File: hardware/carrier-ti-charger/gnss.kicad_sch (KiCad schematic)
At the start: 28 parts, among them J13 GNSS_ANT, Q14 AO3401A, Q15 2N7002, Q16 2N7002, SW5 ACTIVE_ANT, U16 MAX-M10S-00B, U17 TLV9001IDBVR, U18 TPS7A0233PDBVR

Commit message: Fix missing parts.
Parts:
- D11: footprint Diode_SMD:D_0402_1005Metric -> carrier:D_0402_1005Metric
- D12: value BAT54WS -> 1N4148WS; LCSC C22629 -> C2128; MPN BAT54WS -> 1N4148WS
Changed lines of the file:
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@@
 			)
 		)
-		(property "Value" "BAT54WS"
+		(property "Value" "1N4148WS"
 			(at 116.84 41.91 0)
 			(show_name no)
@@
 			)
 		)
-		(property "LCSC" "C22629"
+		(property "LCSC" "C2128"
 			(at 119.38 48.26 0)
 			(hide yes)
@@
 			)
 		)
-		(property "MPN" "BAT54WS"
+		(property "MPN" "1N4148WS"
 			(at 119.38 48.26 0)
 			(hide yes)
@@
 			)
 		)
-		(property "Footprint" "Diode_SMD:D_0402_1005Metric"
+		(property "Footprint" "carrier:D_0402_1005Metric"
 			(at 195.58 107.95 0)
 			(hide yes)

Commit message: Consolidate bom.
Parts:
- C60, C61: value 100n 50V -> 100n 16V; footprint Capacitor_SMD:C_0603_1608Metric -> carrier:C_0402_1005Metric_NoSilk; LCSC C14663 -> C1525; MPN CC0603KRX7R9BB104 -> CL05B104KO5NNNC
- D14: value CT-1608DUPC-P6 -> KT-0603W white; LCSC C52676000 -> C2290; MPN CT-1608DUPC-P6 -> KT-0603W
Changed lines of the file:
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@@
 			)
 		)
-		(property "Value" "100n 50V"
+		(property "Value" "100n 16V"
 			(at 104.14 81.28 0)
 			(show_name no)
@@
 			)
 		)
-		(property "Footprint" "Capacitor_SMD:C_0603_1608Metric"
+		(property "Footprint" "carrier:C_0402_1005Metric_NoSilk"
 			(at 101.6 80.01 0)
 			(hide yes)
@@
 			)
 		)
-		(property "LCSC" "C14663"
+		(property "LCSC" "C1525"
 			(at 101.6 80.01 0)
 			(hide yes)
@@
 			)
 		)
-		(property "MPN" "CC0603KRX7R9BB104"
+		(property "MPN" "CL05B104KO5NNNC"
 			(at 101.6 80.01 0)
 			(hide yes)
@@
 			)
 		)
-		(property "Value" "100n 50V"
+		(property "Value" "100n 16V"
 			(at 231.14 157.48 0)
 			(show_name no)
@@
 			)
 		)
-		(property "Footprint" "Capacitor_SMD:C_0603_1608Metric"
+		(property "Footprint" "carrier:C_0402_1005Metric_NoSilk"
 			(at 228.6 156.21 0)
 			(hide yes)
@@
 			)
 		)
-		(property "LCSC" "C14663"
+		(property "LCSC" "C1525"
 			(at 228.6 156.21 0)
 			(hide yes)
@@
 			)
 		)
-		(property "MPN" "CC0603KRX7R9BB104"
+		(property "MPN" "CL05B104KO5NNNC"
 			(at 228.6 156.21 0)
 			(hide yes)
@@
 			)
 		)
-		(property "Value" "CT-1608DUPC-P6"
+		(property "Value" "KT-0603W white"
 			(at 86.36 152.4 90)
 			(show_name no)
@@
 			)
 		)
-		(property "Description" "Fix LED, purple, blinks with PPS"
+		(property "Description" "Fix LED, white, blinks with PPS"
 			(at 83.82 151.13 0)
 			(hide yes)
@@
 			)
 		)
-		(property "LCSC" "C52676000"
+		(property "LCSC" "C2290"
 			(at 83.82 151.13 0)
 			(hide yes)
@@
 			)
 		)
-		(property "MPN" "CT-1608DUPC-P6"
+		(property "MPN" "KT-0603W"
 			(at 83.82 151.13 0)
 			(hide yes)

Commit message: Address review findings.
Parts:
- R82: LCSC C17415 -> C727983; MPN 0805W8F100JT5E -> AC0805FR-7W10RL
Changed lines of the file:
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@@
 			)
 		)
-		(property "Description" "Antenna current sense and short limit (UBX-20053088 R8)"
+		(property "Description" "Antenna current sense and short limit, 0.25 W (UBX-20053088 R8)"
 			(at 185.42 132.08 0)
 			(hide yes)
@@
 			)
 		)
-		(property "LCSC" "C17415"
+		(property "LCSC" "C727983"
 			(at 185.42 132.08 0)
 			(hide yes)
@@
 			)
 		)
-		(property "MPN" "0805W8F100JT5E"
+		(property "MPN" "AC0805FR-7W10RL"
 			(at 185.42 132.08 0)
 			(hide yes)

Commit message: Polishing.
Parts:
- renumbered J13 to J7, JP4 to JP2

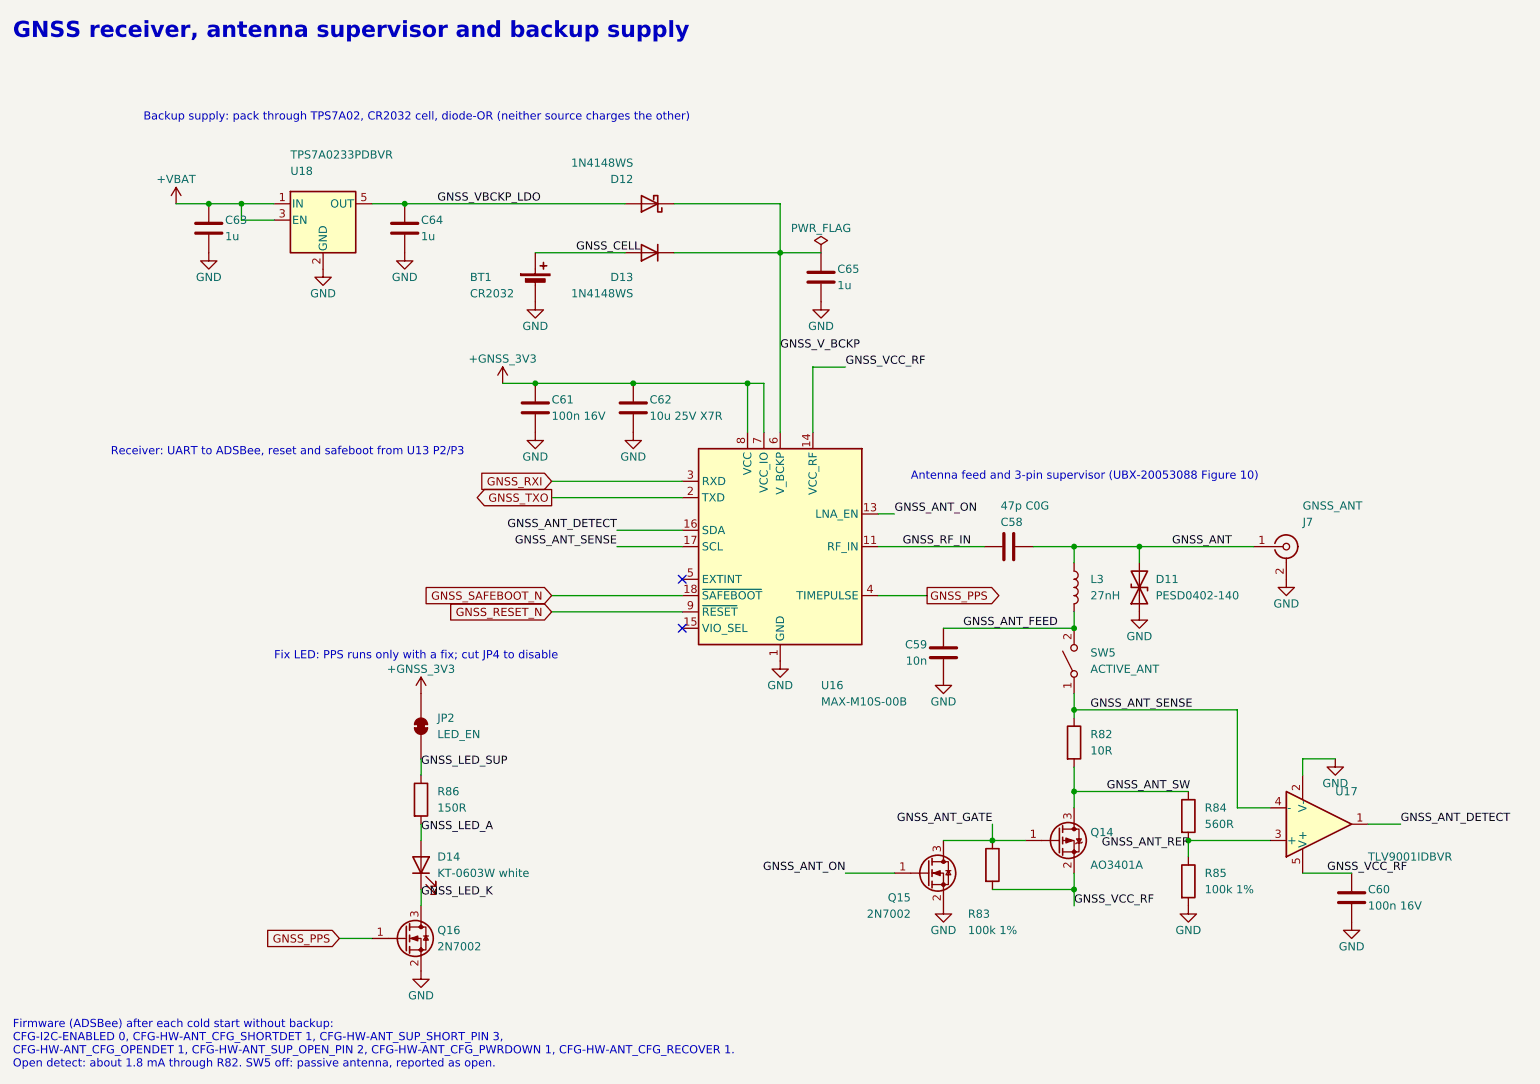
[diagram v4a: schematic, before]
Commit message: Consolidate BOM, add GNSS listen to ESP.
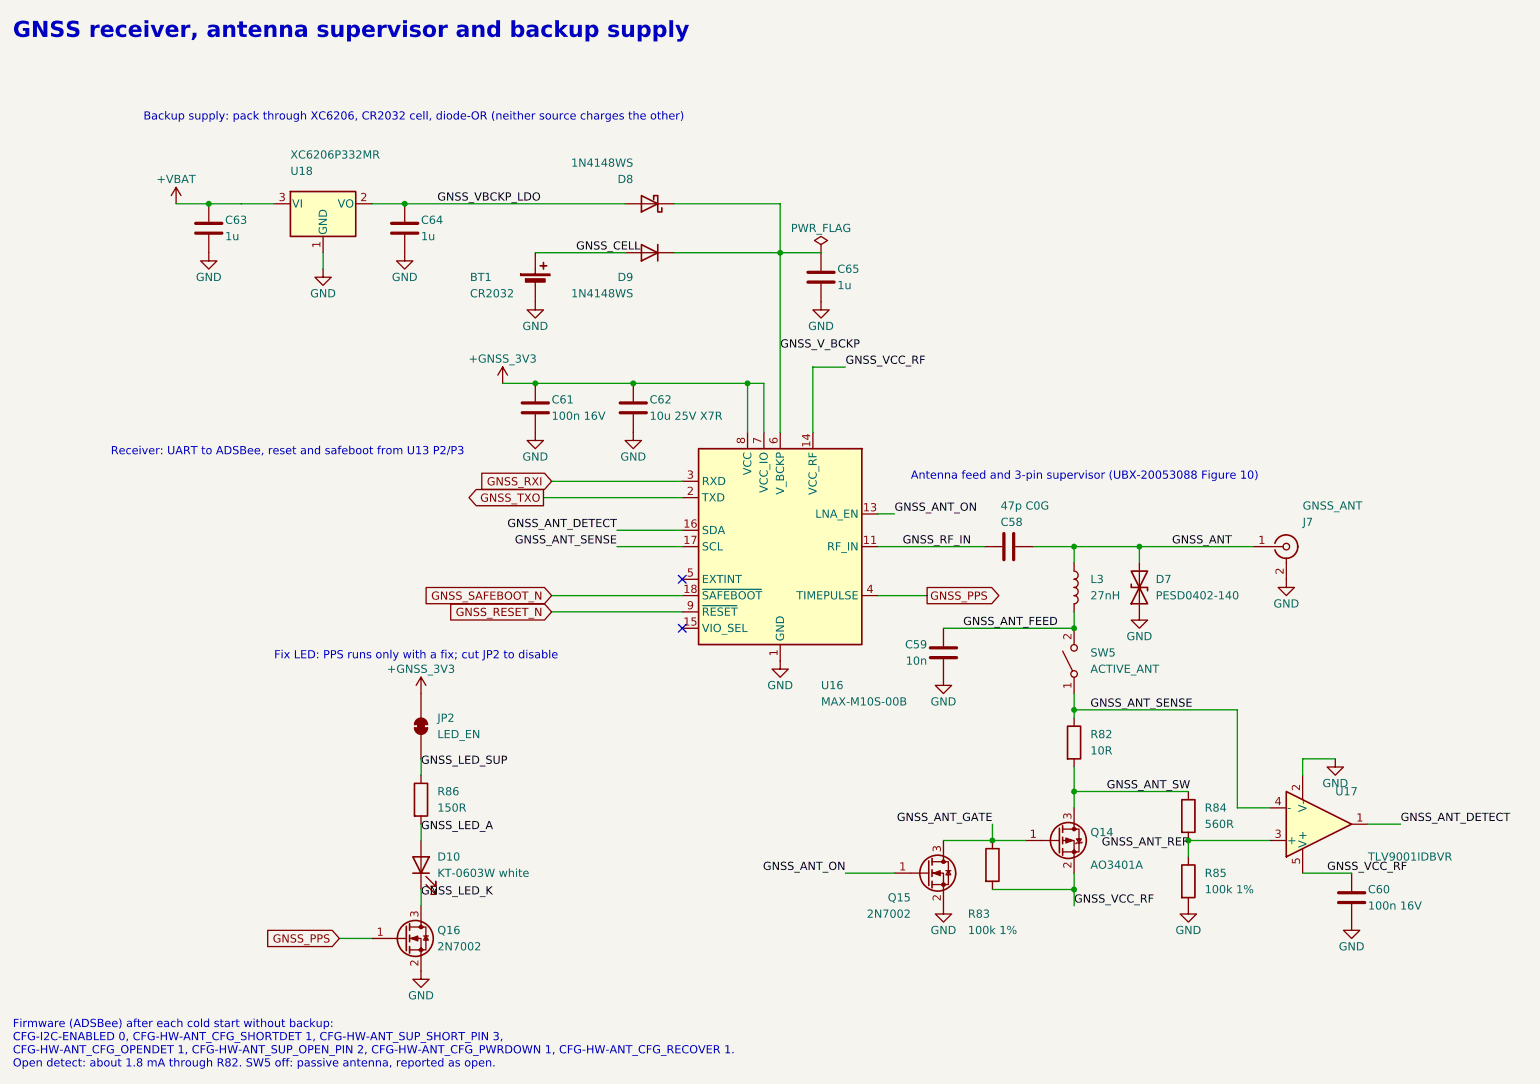
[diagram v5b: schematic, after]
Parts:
- removed U18: TPS7A0233PDBVR, Package_TO_SOT_SMD:SOT-23-5, symbol carrier:TPS7A0233PDBV
- added U18: XC6206P332MR, Package_TO_SOT_SMD:SOT-23, symbol Mark:XC6206P332MR
- BT1: footprint carrier:BAT-SMD_BS-CR2032-8 -> Mark:BAT-SMD_BS-CR2032-8
- C58, C60, C61: footprint carrier:C_0402_1005Metric_NoSilk -> Mark:C_0402_1005Metric_NoSilk
- D7: renamed from D11; footprint carrier:D_0402_1005Metric -> Mark:D_0402_1005Metric
- J7: footprint carrier:U.FL_Hirose_U.FL-R-SMT-1_Vertical -> Mark:U.FL_Hirose_U.FL-R-SMT-1_Vertical
- R82: footprint carrier:R_0805_2012Metric_NoSilk -> Mark:R_0805_2012Metric_NoSilk
- SW5: footprint carrier:SW-SMD_SHOUHAN_2.54-1P_TPGT -> Mark:SW-SMD_SHOUHAN_2.54-1P_TPGT
- U16: footprint carrier:ublox_MAX-M10S -> Mark:ublox_MAX-M10S
- U17: symbol carrier:TLV9001IDBV -> Mark:TLV9001IDBV
- renumbered D14 to D10, D12 to D8, D13 to D9
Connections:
- net +VBAT: now also U18.3 (VI)
- net GND: now also U18.1 (GND)
- net GNSS_VBCKP_LDO: now also U18.2 (VO)
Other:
- note added: "Backup supply: pack through XC6206, CR2032 cell, diode-OR (neither source charges the other)"
- note added: "Fix LED: PPS runs only with a fix; cut JP2 to disable"
- note removed: "Backup supply: pack through TPS7A02, CR2032 cell, diode-OR (neither source charges the other)"
- note removed: "Fix LED: PPS runs only with a fix; cut JP4 to disable"
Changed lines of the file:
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@@
 		)
 	)
-	(text "Backup supply: pack through TPS7A02, CR2032 cell, diode-OR (neither source charges the other)"
+	(text "Backup supply: pack through XC6206, CR2032 cell, diode-OR (neither source charges the other)"
 		(exclude_from_sim no)
 		(at 40.64 35.56 0)
@@
 		)
 	)
-	(text "Fix LED: PPS runs only with a fix; cut JP4 to disable"
+	(text "Fix LED: PPS runs only with a fix; cut JP2 to disable"
 		(exclude_from_sim no)
 		(at 60.96 119.38 0)
@@
 	)
 	(junction
-		(at 55.88 48.26)
-		(diameter 0)
-		(color 0 0 0 0)
-	)
-	(junction
 		(at 50.8 48.26)
 		(diameter 0)
@@
 	(wire
 		(pts
-			(xy 104.14 93.98) (xy 124.46 93.98)
+			(xy 102.87 93.98) (xy 124.46 93.98)
 		)
 		(stroke
@@
 	(wire
 		(pts
-			(xy 55.88 50.8) (xy 60.96 50.8)
-		)
-		(stroke
-			(width 0)
-			(type default)
-		)
-	)
-	(wire
-		(pts
 			(xy 179.07 101.6) (xy 185.42 101.6)
 		)
@@
 	(wire
 		(pts
-			(xy 55.88 48.26) (xy 55.88 50.8)
-		)
-		(stroke
-			(width 0)
-			(type default)
-		)
-	)
-	(wire
-		(pts
 			(xy 124.46 101.6) (xy 114.3 101.6)
 		)
@@
 	(global_label "GNSS_TXO"
 		(shape output)
-		(at 104.14 93.98 180)
+		(at 102.87 93.98 180)
 		(fields_autoplaced yes)
 		(effects
@@
 		)
 		(property "Intersheetrefs" "${INTERSHEET_REFS}"
-			(at 104.14 93.98 0)
+			(at 102.87 93.98 0)
 			(hide yes)
 			(show_name no)
@@
 	)
 	(symbol
-		(lib_id "carrier:+GNSS_3V3")
+		(lib_id "Mark:+GNSS_3V3")
 		(at 83.82 124.46 0)
 		(unit 1)
@@
 			)
 		)
-		(property "Footprint" "carrier:ublox_MAX-M10S"
+		(property "Footprint" "Mark:ublox_MAX-M10S"
 			(at 139.7 101.6 0)
 			(hide yes)
@@
 		(in_pos_files yes)
 		(dnp no)
-		(property "Reference" "D12"
+		(property "Reference" "D8"
 			(at 116.84 44.45 0)
 			(show_name no)
@@
 			(project "carrier"
 				(path "/1d76d2ec-7795-4c71-8167-b1182c3ebc1d/a06322b6-1276-4059-95cd-666fc3516e91"
-					(reference "D12")
+					(reference "D8")
 					(unit 1)
 				)
@@
 	)
 	(symbol
-		(lib_id "carrier:+GNSS_3V3")
+		(lib_id "Mark:+GNSS_3V3")
 		(at 96.52 76.2 0)
 		(unit 1)
@@
 	)
 	(symbol
-		(lib_id "carrier:TLV9001IDBV")
+		(lib_id "Mark:TLV9001IDBV")
 		(at 223.52 144.78 0)
 		(mirror x)
@@
 		(in_pos_files yes)
 		(dnp no)
-		(property "Reference" "D11"
+		(property "Reference" "D7"
 			(at 198.12 106.68 90)
 			(show_name no)
@@
 			)
 		)
-		(property "Footprint" "carrier:D_0402_1005Metric"
+		(property "Footprint" "Mark:D_0402_1005Metric"
 			(at 195.58 107.95 0)
 			(hide yes)
@@
 			(project "carrier"
 				(path "/1d76d2ec-7795-4c71-8167-b1182c3ebc1d/a06322b6-1276-4059-95cd-666fc3516e91"
-					(reference "D11")
+					(reference "D7")
 					(unit 1)
 				)
@@
 	)
 	(symbol
-		(lib_id "carrier:TPS7A0233PDBV")
-		(at 68.58 50.8 0)
-		(unit 1)
-		(body_style 1)
-		(exclude_from_sim no)
-		(in_bom yes)
-		(on_board yes)
-		(in_pos_files yes)
-		(dnp no)
-		(property "Reference" "U18"
-			(at 63.5 43.18 0)
-			(show_name no)
-			(do_not_autoplace no)
-			(effects
-				(font
-					(size 1.27 1.27)
-				)
-				(justify left)
-			)
-		)
-		(property "Value" "TPS7A0233PDBVR"
-			(at 63.5 40.64 0)
-			(show_name no)
-			(do_not_autoplace no)
-			(effects
-				(font
-					(size 1.27 1.27)
-				)
-				(justify left)
-			)
-		)
-		(property "Footprint" "Package_TO_SOT_SMD:SOT-23-5"
-			(at 68.58 50.8 0)
-			(hide yes)
-			(show_name no)
-			(do_not_autoplace no)
-			(effects
-				(font
-					(size 1.27 1.27)
-				)
-			)
-		)
-		(property "Datasheet" "https://www.ti.com/lit/ds/symlink/tps7a02.pdf"
-			(at 68.58 50.8 0)
-			(hide yes)
-			(show_name no)
-			(do_not_autoplace no)
-			(effects
-				(font
-					(size 1.27 1.27)
-				)
-			)
-		)
-		(property "Description" "Always-on 3.3 V backup supply from the pack, 25 nA quiescent"
-			(at 68.58 50.8 0)
-			(hide yes)
-			(show_name no)
-			(do_not_autoplace no)
-			(effects
-				(font
-					(size 1.27 1.27)
-				)
-			)
-		)
-		(property "LCSC" "C2887324"
-			(at 68.58 50.8 0)
-			(hide yes)
-			(show_name no)
-			(do_not_autoplace no)
-			(effects
-				(font
-					(size 1.27 1.27)
-				)
-			)
-		)
-		(property "MPN" "TPS7A0233PDBVR"
-			(at 68.58 50.8 0)
-			(hide yes)
-			(show_name no)
-			(do_not_autoplace no)
-			(effects
-				(font
-					(size 1.27 1.27)
-				)
-			)
-		)
-		(property "Manufacturer" "Texas Instruments"
-			(at 68.58 50.8 0)
-			(hide yes)
-			(show_name no)
-			(do_not_autoplace no)
-			(effects
-				(font
-					(size 1.27 1.27)
-				)
-			)
-		)
-		(pin "1"
-		)
-		(pin "2"
-		)
-		(pin "3"
-		)
-		(pin "4"
-		)
-		(pin "5"
-		)
-		(instances
-			(project "carrier"
-				(path "/1d76d2ec-7795-4c71-8167-b1182c3ebc1d/a06322b6-1276-4059-95cd-666fc3516e91"
-					(reference "U18")
-					(unit 1)
-				)
-			)
-		)
-	)
-	(symbol
 		(lib_id "Device:R")
 		(at 185.42 132.08 0)
@@
 			)
 		)
-		(property "Footprint" "carrier:R_0805_2012Metric_NoSilk"
+		(property "Footprint" "Mark:R_0805_2012Metric_NoSilk"
 			(at 185.42 132.08 0)
 			(hide yes)
@@
 	)
 	(symbol
-		(lib_id "carrier:+VBAT")
+		(lib_id "Mark:+VBAT")
 		(at 45.72 48.26 0)
 		(unit 1)
@@
 			)
 		)
-		(property "Footprint" "carrier:C_0402_1005Metric_NoSilk"
+		(property "Footprint" "Mark:C_0402_1005Metric_NoSilk"
 			(at 101.6 80.01 0)
 			(hide yes)
@@
 			)
 		)
-		(property "Footprint" "carrier:U.FL_Hirose_U.FL-R-SMT-1_Vertical"
+		(property "Footprint" "Mark:U.FL_Hirose_U.FL-R-SMT-1_Vertical"
 			(at 218.44 101.6 0)
 			(hide yes)
@@
 			)
 		)
-		(property "Footprint" "carrier:C_0402_1005Metric_NoSilk"
+		(property "Footprint" "Mark:C_0402_1005Metric_NoSilk"
 			(at 228.6 156.21 0)
 			(hide yes)
@@
 		(in_pos_files yes)
 		(dnp no)
-		(property "Reference" "D14"
+		(property "Reference" "D10"
 			(at 86.36 149.86 90)
 			(show_name no)
@@
 			(project "carrier"
 				(path "/1d76d2ec-7795-4c71-8167-b1182c3ebc1d/a06322b6-1276-4059-95cd-666fc3516e91"
-					(reference "D14")
+					(reference "D10")
 					(unit 1)
 				)
@@
 			)
 		)
-		(property "Footprint" "carrier:BAT-SMD_BS-CR2032-8"
+		(property "Footprint" "Mark:BAT-SMD_BS-CR2032-8"
 			(at 101.6 60.96 0)
 			(hide yes)
@@
 			)
 		)
-		(property "Footprint" "carrier:C_0402_1005Metric_NoSilk"
+		(property "Footprint" "Mark:C_0402_1005Metric_NoSilk"
 			(at 175.26 101.6 0)
 			(hide yes)
@@
 			)
 		)
-		(property "Footprint" "carrier:SW-SMD_SHOUHAN_2.54-1P_TPGT"
+		(property "Footprint" "Mark:SW-SMD_SHOUHAN_2.54-1P_TPGT"
 			(at 185.42 119.38 0)
 			(hide yes)
@@
 		(in_pos_files yes)
 		(dnp no)
-		(property "Reference" "D13"
+		(property "Reference" "D9"
 			(at 116.84 59.69 0)
 			(show_name no)
@@
 			(project "carrier"
 				(path "/1d76d2ec-7795-4c71-8167-b1182c3ebc1d/a06322b6-1276-4059-95cd-666fc3516e91"
-					(reference "D13")
+					(reference "D9")
 					(unit 1)
 				)
@@
 		)
 	)
+	(symbol
+		(lib_id "Mark:XC6206P332MR")
+		(at 68.58 48.26 0)
+		(unit 1)
+		(body_style 1)
+		(exclude_from_sim no)
+		(in_bom yes)
+		(on_board yes)
+		(in_pos_files yes)
+		(dnp no)
+		(property "Reference" "U18"
+			(at 63.5 43.18 0)
+			(show_name no)
+			(do_not_autoplace no)
+			(effects
+				(font
+					(size 1.27 1.27)
+				)
+				(justify left)
+			)
+		)
+		(property "Value" "XC6206P332MR"
+			(at 63.5 40.64 0)
+			(show_name no)
+			(do_not_autoplace no)
+			(effects
+				(font
+					(size 1.27 1.27)
+				)
+				(justify left)
+			)
+		)
+		(property "Footprint" "Package_TO_SOT_SMD:SOT-23"
+			(at 68.58 48.26 0)
+			(hide yes)
+			(show_name no)
+			(do_not_autoplace no)
+			(effects
+				(font
+					(size 1.27 1.27)
+				)
+			)
+		)
+		(property "Datasheet" "https://www.torexsemi.com/file/xc6206/XC6206.pdf"
+			(at 68.58 48.26 0)
+			(hide yes)
+			(show_name no)
+			(do_not_autoplace no)
+			(effects
+				(font
+					(size 1.27 1.27)
+				)
+			)
+		)
+		(property "Description" "Always-on 3.3 V backup supply from the pack, about 1 uA quiescent"
+			(at 68.58 48.26 0)
+			(hide yes)
+			(show_name no)
+			(do_not_autoplace no)
+			(effects
+				(font
+					(size 1.27 1.27)
+				)
+			)
+		)
+		(property "LCSC" "C5446"
+			(at 68.58 48.26 0)
+			(hide yes)
+			(show_name no)
+			(do_not_autoplace no)
+			(effects
+				(font
+					(size 1.27 1.27)
+				)
+			)
+		)
+		(property "MPN" "XC6206P332MR"
+			(at 68.58 48.26 0)
+			(hide yes)
+			(show_name no)
+			(do_not_autoplace no)
+			(effects
+				(font
+					(size 1.27 1.27)
+				)
+			)
+		)
+		(property "Manufacturer" "Torex"
+			(at 68.58 48.26 0)
+			(hide yes)
+			(show_name no)
+			(do_not_autoplace no)
+			(effects
+				(font
+					(size 1.27 1.27)
+				)
+			)
+		)
+		(pin "1"
+		)
+		(pin "2"
+		)
+		(pin "3"
+		)
+		(instances
+			(project "carrier"
+				(path "/1d76d2ec-7795-4c71-8167-b1182c3ebc1d/a06322b6-1276-4059-95cd-666fc3516e91"
+					(reference "U18")
+					(unit 1)
+				)
+			)
+		)
+	)
+	(wire
+		(pts
+			(xy 68.58 55.88) (xy 68.58 58.42)
+		)
+		(stroke
+			(width 0)
+			(type default)
+		)
+	)
